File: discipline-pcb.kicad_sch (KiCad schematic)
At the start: 150 parts, among them SW1 KEYSW, SW10 KEYSW, SW11 KEYSW, SW12 KEYSW, SW13 KEYSW, SW14 KEYSW, SW15 KEYSW, SW16 KEYSW, SW17 KEYSW, SW18 KEYSW, SW19 KEYSW, SW2 KEYSW, SW20 KEYSW, SW21 KEYSW, SW22 KEYSW, SW23 KEYSW, SW24 KEYSW, SW25 KEYSW, SW26 KEYSW, SW27 KEYSW, SW28 KEYSW, SW29 KEYSW, SW3 KEYSW, SW30 KEYSW, SW31 KEYSW, SW32 KEYSW, SW33 KEYSW, SW34 KEYSW, SW35 KEYSW, SW36 KEYSW, SW37 KEYSW, SW38 KEYSW, SW39 KEYSW, SW4 KEYSW, SW40 KEYSW, SW41 KEYSW, SW42 KEYSW, SW43 KEYSW, SW44 KEYSW, SW45 KEYSW, SW46 KEYSW, SW47 KEYSW, SW48 KEYSW, SW49 KEYSW, SW5 KEYSW, SW50 KEYSW, SW51 KEYSW, SW52 KEYSW, SW53 KEYSW, SW54 KEYSW, SW55 KEYSW, SW56 KEYSW, SW57 KEYSW, SW58 KEYSW, SW59 KEYSW, SW6 KEYSW, SW60 KEYSW, SW61 KEYSW, SW62 KEYSW, SW63 KEYSW, SW64 KEYSW, SW65 KEYSW, SW66 KEYSW, SW67 KEYSW, SW68 KEYSW, SW69 KEYSW, SW7 KEYSW, SW70 KEYSW, SW71 KEYSW, SW72 KEYSW, SW73 KEYSW, SW74 KEYSW, SW75 KEYSW, SW76 KEYSW, SW77 KEYSW, SW78 KEYSW, SW79 SW_SPST, SW8 KEYSW, SW9 KEYSW, U1 SuperMini nRF52840

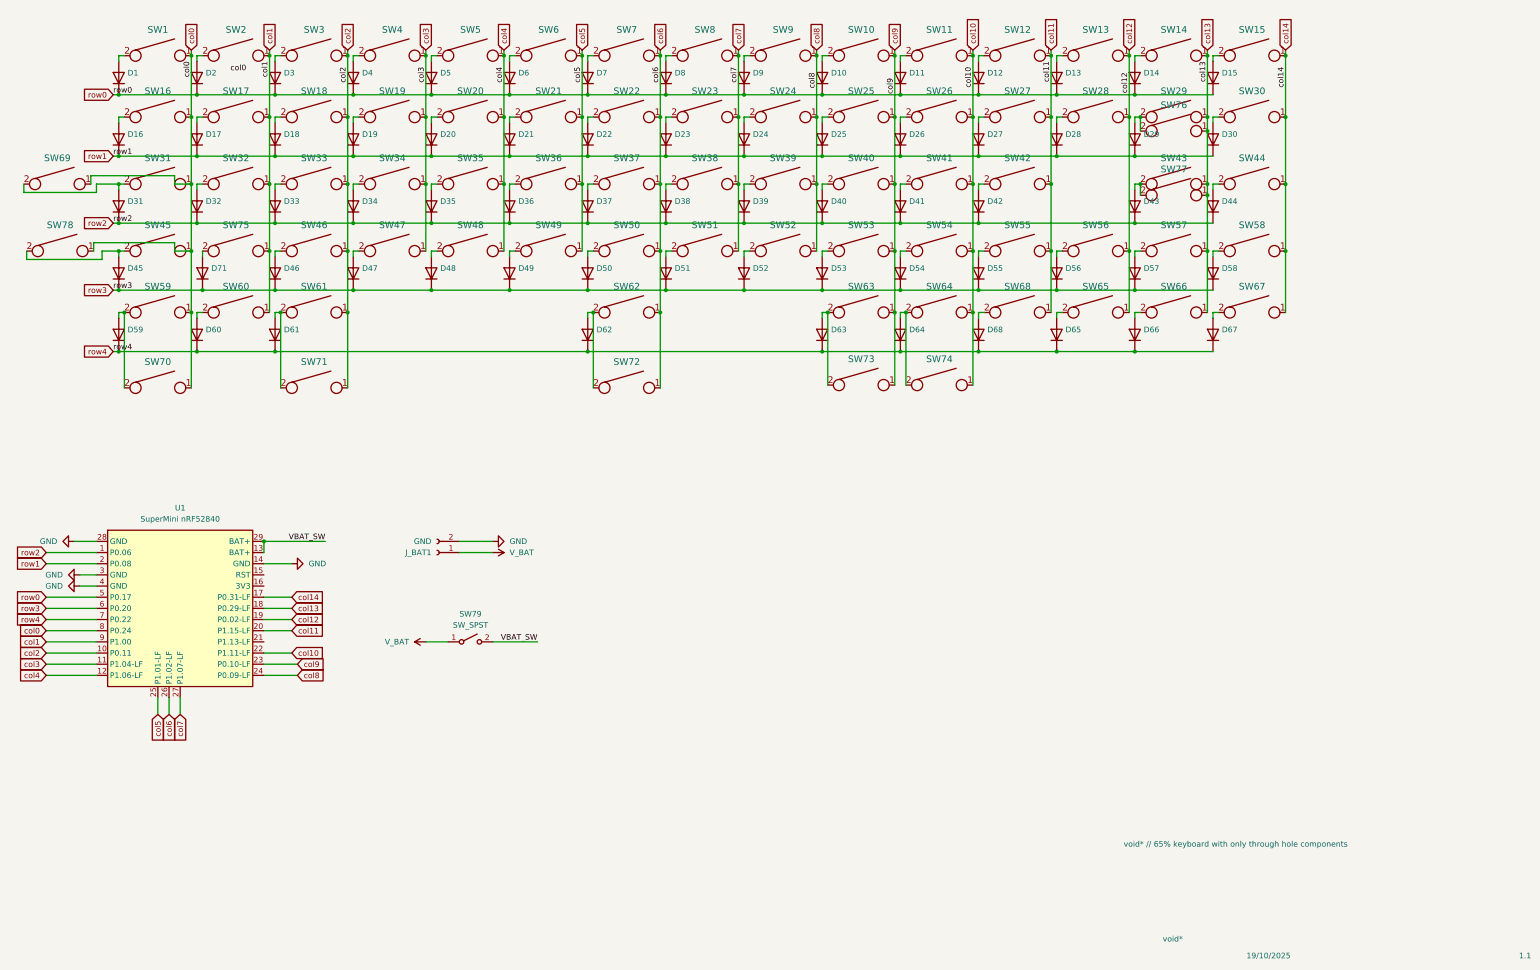
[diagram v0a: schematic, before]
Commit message: Finishing JLCPCB support and implementing decoupling capacitors
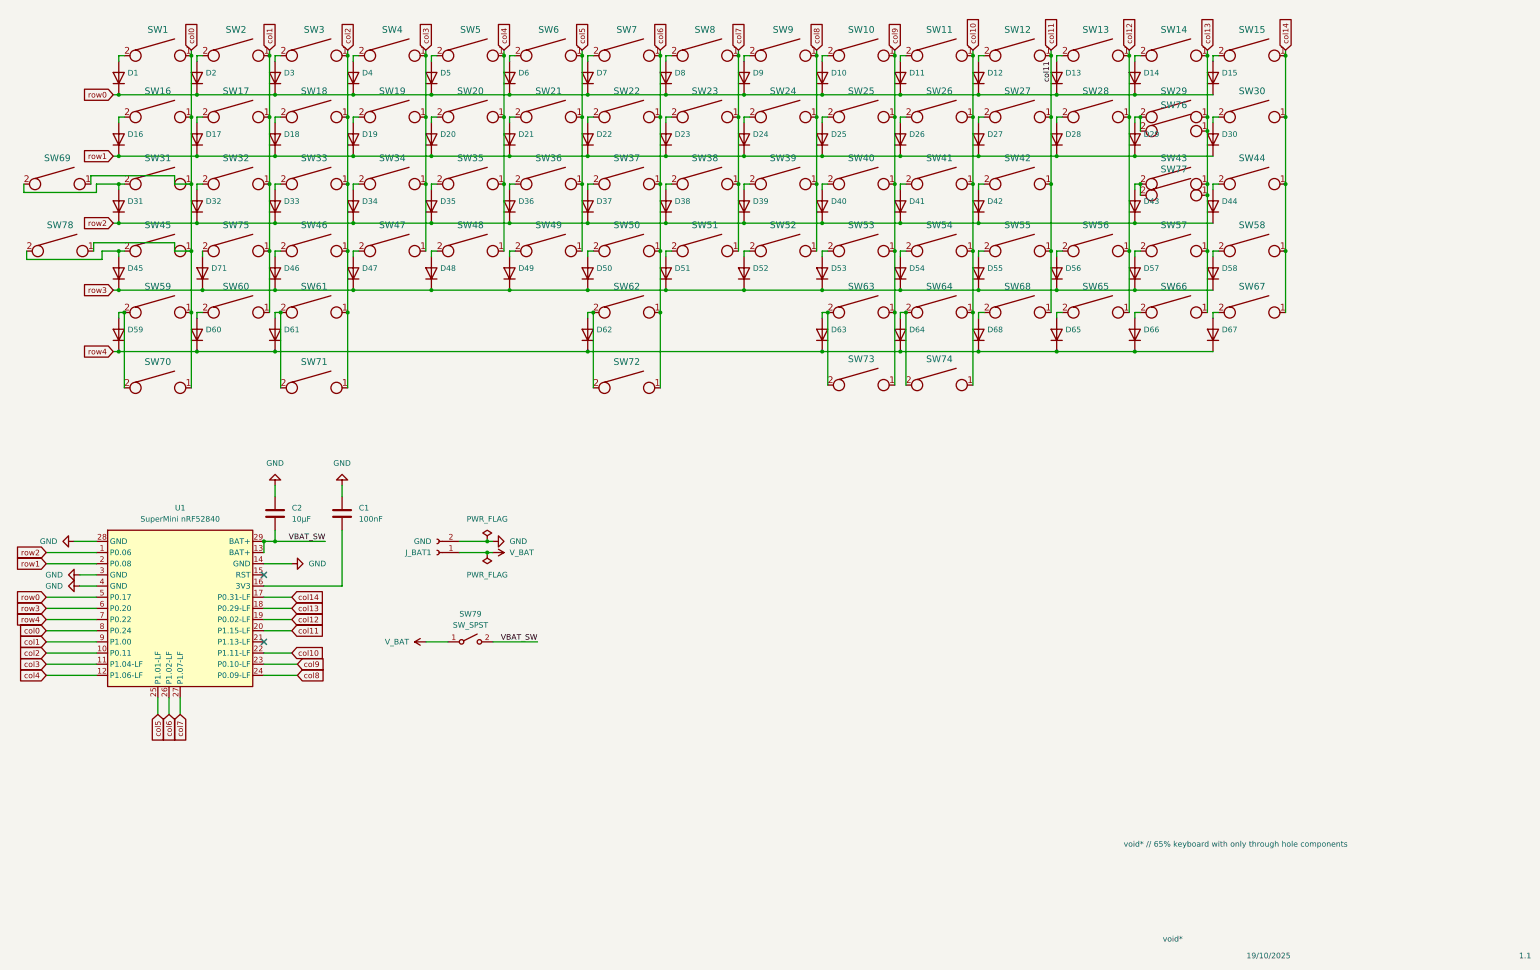
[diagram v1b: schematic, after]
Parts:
- added C1: 100nF, Capacitor_THT:C_Rect_L11.5mm_W5.2mm_P10.00mm_MKT, symbol Device:C
- added C2: 10µF, Capacitor_THT:C_Disc_D4.7mm_W2.5mm_P5.00mm, symbol Device:C
- U1: footprint marbastlib-xp-promicroish:SuperMini_nRF52840_AH_USBup -> PCM_marbastlib-xp-promicroish:SuperMini_nRF52840_AH_USBup
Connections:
- net GND: now also C1.2, C2.1
- net VBAT_SW: now also C2.2
- net at U1.16 (3V3): now also C1.1
- no-connect marks 0 -> 2

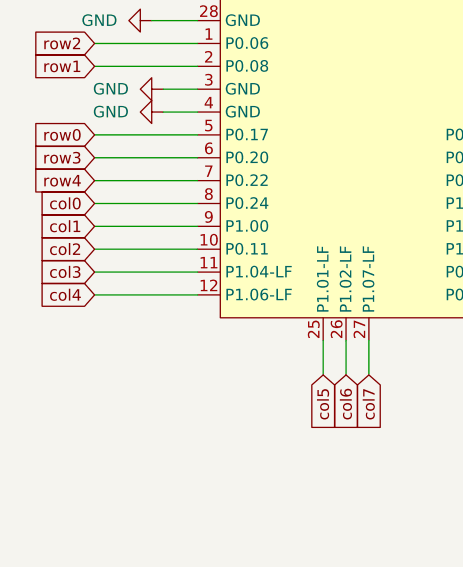
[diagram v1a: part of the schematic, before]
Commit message: Adding GND plane to back layer and rerouting
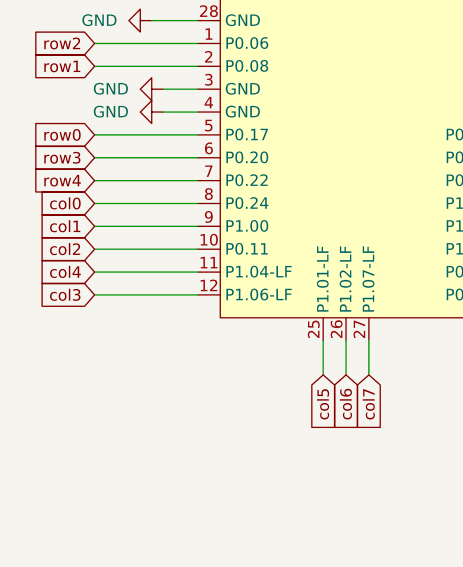
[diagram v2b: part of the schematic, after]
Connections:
- net col3: now also U1.12 (P1.06-LF); no longer U1.11 (P1.04-LF)
- net col4: now also U1.11 (P1.04-LF); no longer U1.12 (P1.06-LF)
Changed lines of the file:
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@@
 	(wire
 		(pts
+			(xy 57.15 213.36) (xy 68.58 213.36)
+		)
+		(stroke
+			(width 0)
+			(type default)
+		)
+	)
+	(wire
+		(pts
 			(xy 270.51 104.14) (xy 269.24 104.14)
 		)
@@
 	(wire
 		(pts
+			(xy 57.15 215.9) (xy 68.58 215.9)
+		)
+		(stroke
+			(width 0)
+			(type default)
+		)
+	)
+	(wire
+		(pts
 			(xy 86.36 102.235) (xy 86.36 104.14)
 		)
@@
 	(wire
 		(pts
-			(xy 57.15 213.36) (xy 68.58 213.36)
-		)
-		(stroke
-			(width 0)
-			(type default)
-		)
-	)
-	(wire
-		(pts
 			(xy 217.17 88.9) (xy 215.9 88.9)
 		)
@@
 	(wire
 		(pts
-			(xy 57.15 215.9) (xy 68.58 215.9)
-		)
-		(stroke
-			(width 0)
-			(type default)
-		)
-	)
-	(wire
-		(pts
 			(xy 198.12 104.14) (xy 198.12 105.41)
 		)
@@
 	(global_label "col3"
 		(shape input)
-		(at 57.15 213.36 180)
+		(at 57.15 215.9 180)
 		(effects
 			(font
@@
 		)
 		(property "Intersheetrefs" "${INTERSHEET_REFS}"
-			(at 57.15 213.36 90)
+			(at 57.15 215.9 90)
 			(effects
 				(font
@@
 	(global_label "col4"
 		(shape input)
-		(at 57.15 215.9 180)
+		(at 57.15 213.36 180)
 		(effects
 			(font
@@
 		)
 		(property "Intersheetrefs" "${INTERSHEET_REFS}"
-			(at 57.15 215.9 90)
+			(at 57.15 213.36 90)
 			(effects
 				(font
